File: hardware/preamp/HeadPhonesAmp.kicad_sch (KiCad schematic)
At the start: 28 parts

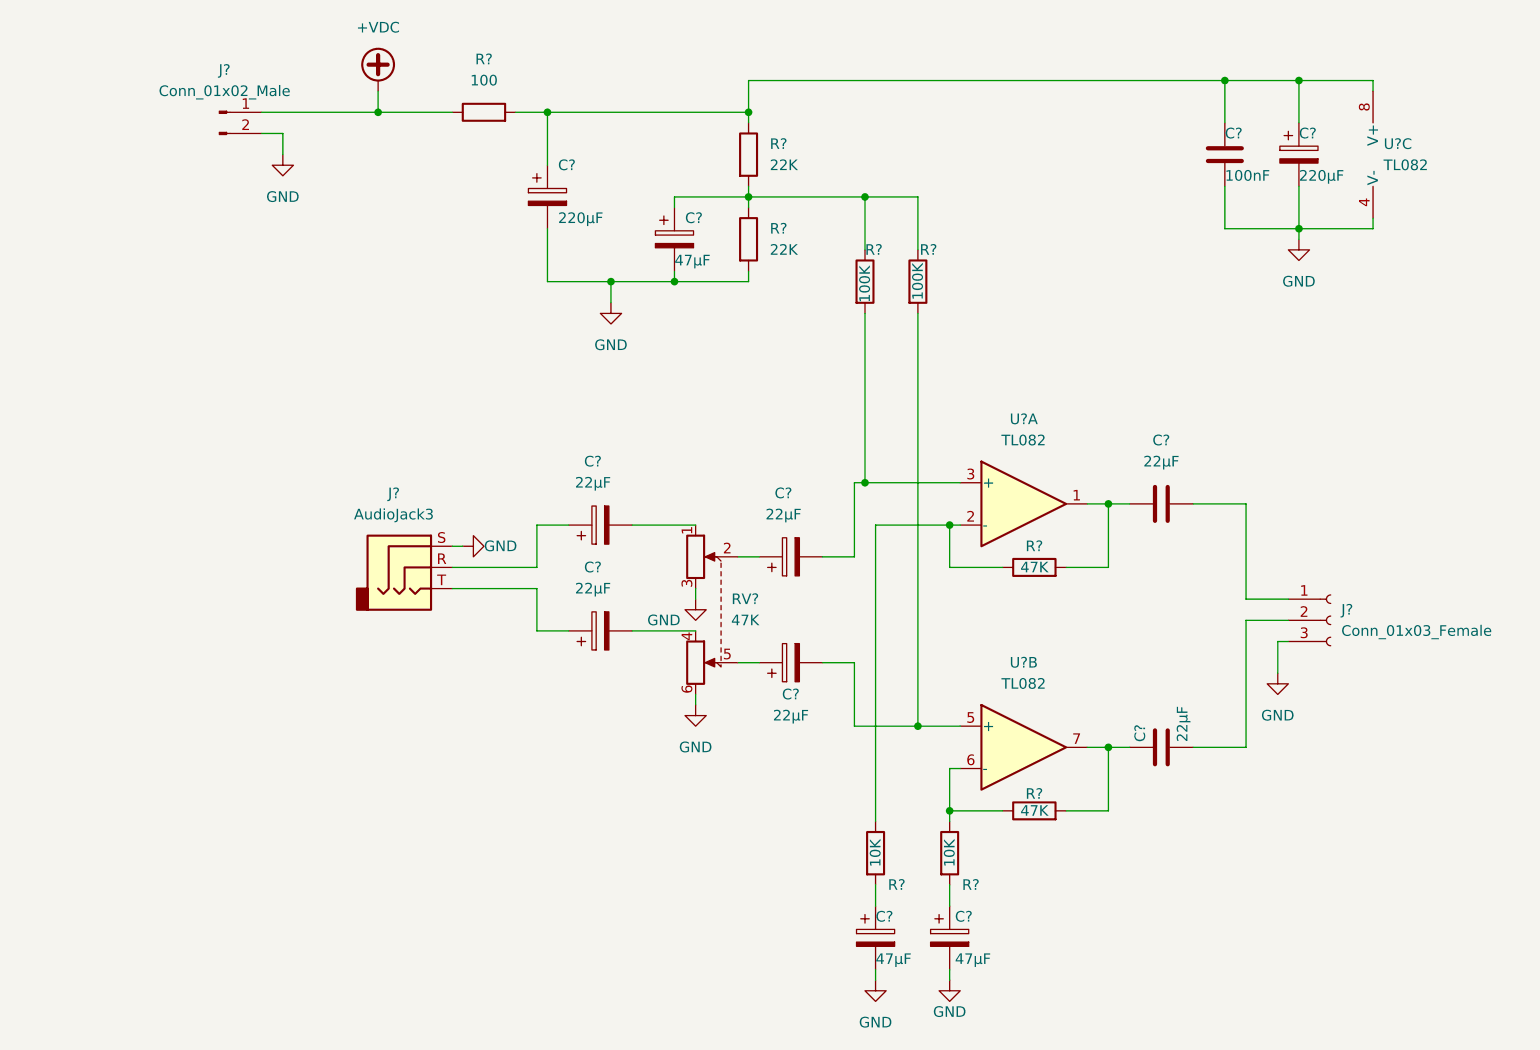
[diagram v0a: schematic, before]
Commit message: amplifier schema almost finished
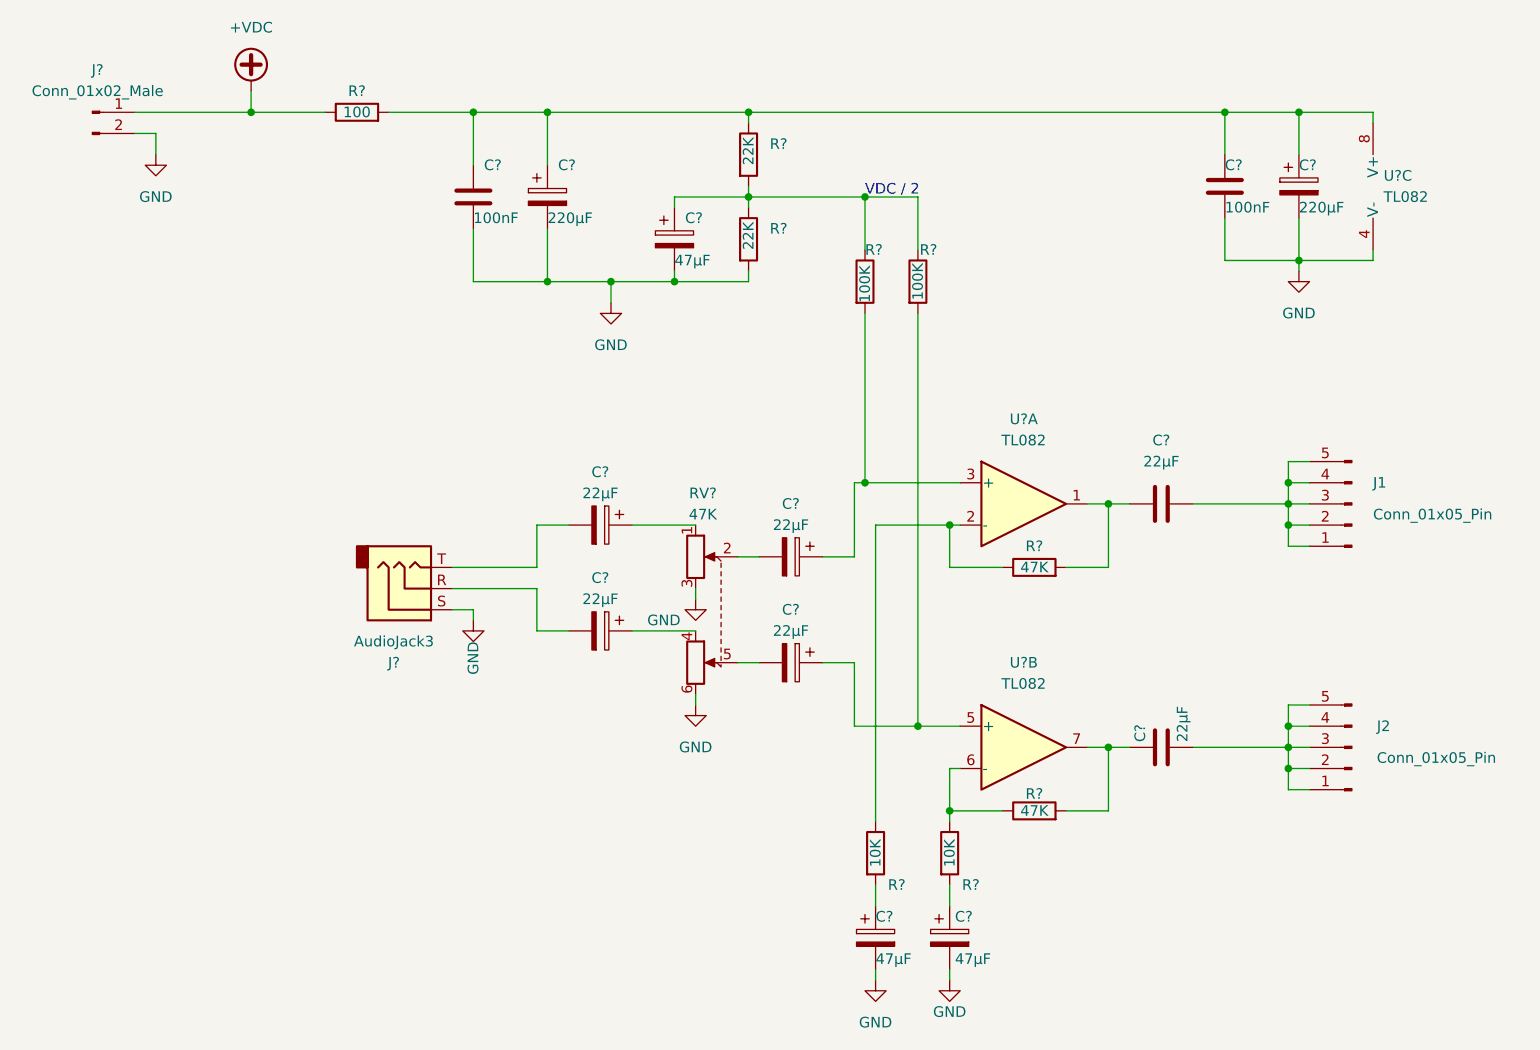
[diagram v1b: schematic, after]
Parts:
- removed J?: Conn_01x03_Female, symbol Connector:Conn_01x03_Female
- added C?: 100nF, symbol Device:C
- added J1, J2: Conn_01x05_Pin, symbol Connector:Conn_01x05_Pin
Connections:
- net GND: now also C?.2
- net at C?.1, C?.1, C?.1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: now also C?.1
- net at C?.1: now also RV?.4; no longer J?.T
- net at C?.2: now also J?.R; no longer RV?.4
- net at R?.2, U?.5 (+): now also C?.1; no longer C?.2
- net at C?.2: now also J1.1 (Pin_1), J1.2 (Pin_2), J1.3 (Pin_3), J1.4 (Pin_4), J1.5 (Pin_5)
- net at C?.2: now also J2.1 (Pin_1), J2.2 (Pin_2), J2.3 (Pin_3), J2.4 (Pin_4), J2.5 (Pin_5)
- net at RV?.1: now also C?.1; no longer C?.2
- net at RV?.2: now also C?.2; no longer C?.1
- net at RV?.5: now also C?.2; no longer C?.1
- net at R?.2, U?.3 (+): now also C?.1; no longer C?.2
- new net: C?.2, J?.T
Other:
- note added: "VDC / 2"
- moved on the sheet: C?, J?, R?, U?C
